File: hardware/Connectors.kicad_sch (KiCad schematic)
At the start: 9 parts, among them J1 Harw_Conn_1x2, J10 USB_B_Mini, J14 Conn_01x05, J16 Harw_Conn_2x13, J2 Harw_Conn_1x2, J3 Harw_Conn_1x2, J8 Harw_Conn_1x4

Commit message: finished board design
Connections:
- net AMS_FAULT_COCKPIT: now also J16.10; no longer J16.22
- net AMS_SAFETY_1: now also J16.9; no longer J16.24
- net AMS_SAFETY_2: now also J16.22; no longer J16.9
- net CAN_H: now also J16.24; no longer J16.10
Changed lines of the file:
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@@
     (stroke (width 0) (type default) (color 0 0 0 0))
   )
-  (wire (pts (xy 84.455 121.92) (xy 81.915 121.92))
+  (wire (pts (xy 66.675 116.84) (xy 69.215 116.84))
     (stroke (width 0) (type default) (color 0 0 0 0))
   )
@@
     (stroke (width 0) (type default) (color 0 0 0 0))
   )
+  (wire (pts (xy 84.455 121.92) (xy 81.915 121.92))
+    (stroke (width 0) (type default) (color 0 0 0 0))
+  )
+  (wire (pts (xy 240.665 63.5) (xy 240.665 64.77))
+    (stroke (width 0) (type default) (color 0 0 0 0))
+  )
+  (wire (pts (xy 250.825 46.99) (xy 250.825 43.18))
+    (stroke (width 0) (type default) (color 0 0 0 0))
+  )
+  (wire (pts (xy 180.975 137.16) (xy 178.435 137.16))
+    (stroke (width 0) (type default) (color 0 0 0 0))
+  )
+  (wire (pts (xy 250.19 111.76) (xy 250.19 113.03))
+    (stroke (width 0) (type default) (color 0 0 0 0))
+  )
+  (wire (pts (xy 179.705 134.62) (xy 179.705 132.08))
+    (stroke (width 0) (type default) (color 0 0 0 0))
+  )
+  (wire (pts (xy 240.665 63.5) (xy 241.935 63.5))
+    (stroke (width 0) (type default) (color 0 0 0 0))
+  )
+  (wire (pts (xy 66.675 104.14) (xy 69.215 104.14))
+    (stroke (width 0) (type default) (color 0 0 0 0))
+  )
+  (wire (pts (xy 69.215 121.92) (xy 66.675 121.92))
+    (stroke (width 0) (type default) (color 0 0 0 0))
+  )
+  (wire (pts (xy 172.72 81.915) (xy 175.26 81.915))
+    (stroke (width 0) (type default) (color 0 0 0 0))
+  )
+  (wire (pts (xy 188.595 47.625) (xy 186.055 47.625))
+    (stroke (width 0) (type default) (color 0 0 0 0))
+  )
+  (wire (pts (xy 249.555 46.99) (xy 250.825 46.99))
+    (stroke (width 0) (type default) (color 0 0 0 0))
+  )
+  (wire (pts (xy 248.92 106.045) (xy 251.46 106.045))
+    (stroke (width 0) (type default) (color 0 0 0 0))
+  )
+  (wire (pts (xy 184.785 48.895) (xy 186.055 48.895))
+    (stroke (width 0) (type default) (color 0 0 0 0))
+  )
   (wire (pts (xy 66.675 119.38) (xy 69.215 119.38))
-    (stroke (width 0) (type default) (color 0 0 0 0))
-  )
-  (wire (pts (xy 240.665 63.5) (xy 240.665 64.77))
-    (stroke (width 0) (type default) (color 0 0 0 0))
-  )
-  (wire (pts (xy 250.825 46.99) (xy 250.825 43.18))
-    (stroke (width 0) (type default) (color 0 0 0 0))
-  )
-  (wire (pts (xy 180.975 137.16) (xy 178.435 137.16))
-    (stroke (width 0) (type default) (color 0 0 0 0))
-  )
-  (wire (pts (xy 250.19 111.76) (xy 250.19 113.03))
-    (stroke (width 0) (type default) (color 0 0 0 0))
-  )
-  (wire (pts (xy 179.705 134.62) (xy 179.705 132.08))
-    (stroke (width 0) (type default) (color 0 0 0 0))
-  )
-  (wire (pts (xy 240.665 63.5) (xy 241.935 63.5))
-    (stroke (width 0) (type default) (color 0 0 0 0))
-  )
-  (wire (pts (xy 66.675 104.14) (xy 69.215 104.14))
-    (stroke (width 0) (type default) (color 0 0 0 0))
-  )
-  (wire (pts (xy 69.215 121.92) (xy 66.675 121.92))
-    (stroke (width 0) (type default) (color 0 0 0 0))
-  )
-  (wire (pts (xy 172.72 81.915) (xy 175.26 81.915))
-    (stroke (width 0) (type default) (color 0 0 0 0))
-  )
-  (wire (pts (xy 188.595 47.625) (xy 186.055 47.625))
-    (stroke (width 0) (type default) (color 0 0 0 0))
-  )
-  (wire (pts (xy 249.555 46.99) (xy 250.825 46.99))
-    (stroke (width 0) (type default) (color 0 0 0 0))
-  )
-  (wire (pts (xy 248.92 106.045) (xy 251.46 106.045))
-    (stroke (width 0) (type default) (color 0 0 0 0))
-  )
-  (wire (pts (xy 184.785 48.895) (xy 186.055 48.895))
-    (stroke (width 0) (type default) (color 0 0 0 0))
-  )
-  (wire (pts (xy 84.455 116.84) (xy 81.915 116.84))
     (stroke (width 0) (type default) (color 0 0 0 0))
   )
@@
     (stroke (width 0) (type default) (color 0 0 0 0))
   )
-  (wire (pts (xy 69.215 116.84) (xy 66.675 116.84))
+  (wire (pts (xy 81.915 116.84) (xy 84.455 116.84))
     (stroke (width 0) (type default) (color 0 0 0 0))
   )
@@
     )
   )
-  (global_label "CAN_H" (shape input) (at 66.675 119.38 180) (fields_autoplaced)
-    (effects (font (size 1.27 1.27)) (justify right))
-    (property "Intersheet References" "${INTERSHEET_REFS}" (id 0) (at 58.3637 119.4594 0)
-      (effects (font (size 1.27 1.27)) (justify right) hide)
+  (global_label "CAN_H" (shape input) (at 84.455 121.92 0) (fields_autoplaced)
+    (effects (font (size 1.27 1.27)) (justify left))
+    (property "Intersheet References" "${INTERSHEET_REFS}" (id 0) (at 92.7663 121.8406 0)
+      (effects (font (size 1.27 1.27)) (justify left) hide)
     )
   )
@@
     )
   )
-  (global_label "AMS_FAULT_COCKPIT" (shape input) (at 84.455 116.84 0) (fields_autoplaced)
-    (effects (font (size 1.27 1.27)) (justify left))
-    (property "Intersheet References" "${INTERSHEET_REFS}" (id 0) (at 105.9502 116.7606 0)
-      (effects (font (size 1.27 1.27)) (justify left) hide)
+  (global_label "AMS_FAULT_COCKPIT" (shape input) (at 66.675 119.38 180) (fields_autoplaced)
+    (effects (font (size 1.27 1.27)) (justify right))
+    (property "Intersheet References" "${INTERSHEET_REFS}" (id 0) (at 45.1798 119.4594 0)
+      (effects (font (size 1.27 1.27)) (justify right) hide)
     )
   )
@@
     )
   )
-  (global_label "AMS_SAFETY_2" (shape input) (at 66.675 116.84 180) (fields_autoplaced)
+  (global_label "AMS_SAFETY_2" (shape input) (at 84.455 116.84 0) (fields_autoplaced)
+    (effects (font (size 1.27 1.27)) (justify left))
+    (property "Intersheet References" "${INTERSHEET_REFS}" (id 0) (at 100.2654 116.7606 0)
+      (effects (font (size 1.27 1.27)) (justify left) hide)
+    )
+  )
+  (global_label "SWDIO" (shape input) (at 178.435 142.24 180) (fields_autoplaced)
+    (effects (font (size 1.27 1.27)) (justify right))
+    (property "Intersheet References" "${INTERSHEET_REFS}" (id 0) (at 170.2446 142.1606 0)
+      (effects (font (size 1.27 1.27)) (justify right) hide)
+    )
+  )
+  (global_label "AIR_M" (shape input) (at 66.675 111.76 180) (fields_autoplaced)
+    (effects (font (size 1.27 1.27)) (justify right))
+    (property "Intersheet References" "${INTERSHEET_REFS}" (id 0) (at 58.9684 111.8394 0)
+      (effects (font (size 1.27 1.27)) (justify right) hide)
+    )
+  )
+  (global_label "AMS_SAFETY_1" (shape input) (at 66.675 116.84 180) (fields_autoplaced)
     (effects (font (size 1.27 1.27)) (justify right))
     (property "Intersheet References" "${INTERSHEET_REFS}" (id 0) (at 50.8646 116.9194 0)
@@
     )
   )
-  (global_label "SWDIO" (shape input) (at 178.435 142.24 180) (fields_autoplaced)
-    (effects (font (size 1.27 1.27)) (justify right))
-    (property "Intersheet References" "${INTERSHEET_REFS}" (id 0) (at 170.2446 142.1606 0)
-      (effects (font (size 1.27 1.27)) (justify right) hide)
-    )
-  )
-  (global_label "AIR_M" (shape input) (at 66.675 111.76 180) (fields_autoplaced)
-    (effects (font (size 1.27 1.27)) (justify right))
-    (property "Intersheet References" "${INTERSHEET_REFS}" (id 0) (at 58.9684 111.8394 0)
-      (effects (font (size 1.27 1.27)) (justify right) hide)
-    )
-  )
-  (global_label "AMS_SAFETY_1" (shape input) (at 84.455 121.92 0) (fields_autoplaced)
-    (effects (font (size 1.27 1.27)) (justify left))
-    (property "Intersheet References" "${INTERSHEET_REFS}" (id 0) (at 100.2654 121.8406 0)
-      (effects (font (size 1.27 1.27)) (justify left) hide)
-    )
-  )

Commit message: schematic override, just cuz
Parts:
- removed J1: Harw_Conn_1x2, M808420245, symbol Harwin 2 pin 90 deg:Harw_Conn_1x2
- removed J10: USB_B_Mini, Connector_USB:USB_Mini-B_Lumberg_2486_01_Horizontal, symbol Connector:USB_B_Mini
- removed R46: 100k, Resistor_SMD:R_0603_1608Metric, symbol Device:R_Small
- added P3: USB_C_Plug_USB2.0, Connector_USB:USB_C_Receptacle_HRO_TYPE-C-31-M-12, symbol Connector:USB_C_Plug_USB2.0
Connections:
- net D+: now also J8.3, P3.A6 (D+); no longer J8.2
- net D-: now also J8.2, P3.A7 (D-); no longer J8.3
- net GND: now also J16.14, J16.15; no longer J16.17, J16.19, J16.8
- net LTC_1_CHASSIS: no longer J16.16
- net LTC_1_OUT_I+: no longer J16.14
- net LTC_1_OUT_I-: no longer J16.1
- net LTC_2_CHASSIS: no longer J16.3
- net LTC_2_OUT_I+: no longer J16.15
- net LTC_2_OUT_I-: no longer J16.2
- net SENSOR_SIGNAL: no longer J16.4
- net USB_GND: now also P3.A1 (GND), P3.A12 (GND), P3.B1 (GND), P3.B12 (GND)
- net VBUS: now also P3.A4 (VBUS), P3.A9 (VBUS), P3.B4 (VBUS), P3.B9 (VBUS)
- net VDD: now also J16.1; no longer J16.21
- net at F1.2: now also J16.2; no longer J16.5
- net HV_ACU_VOLTAGE renamed HV_ACU+
- net HV_ACU+: no longer J3.2
- net HV_CAR_VOLTAGE renamed HV_CAR+
- net HV_CAR+: no longer J2.2
- new net HV_ACU-: J3.2
- new net HV_CAR-: J2.2
- no-connect marks 0 -> 3
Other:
- moved on the sheet: F1

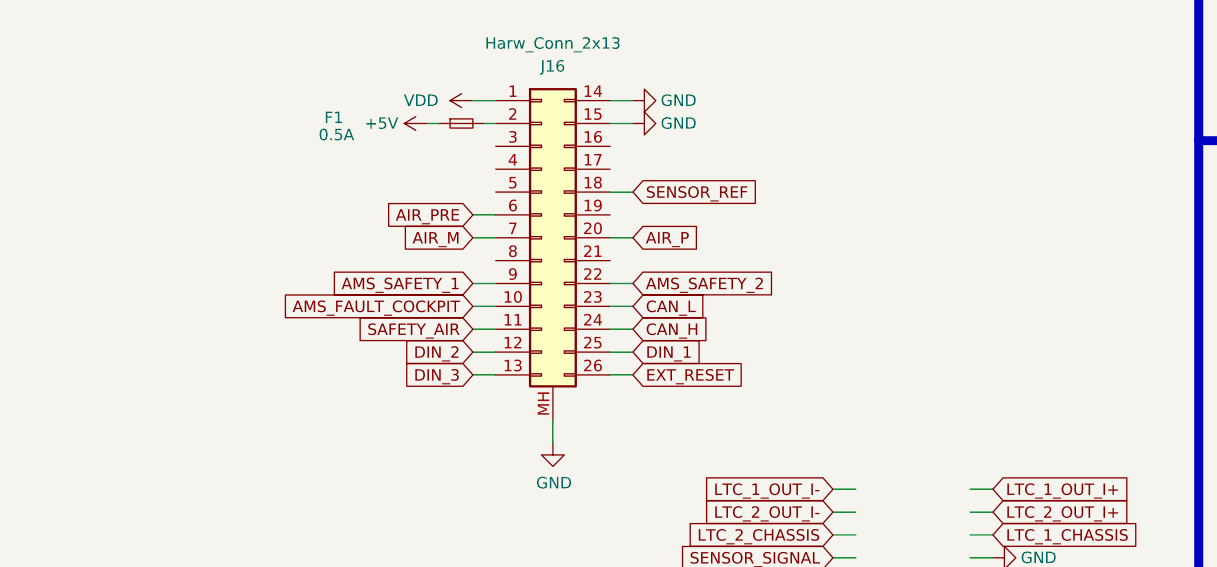
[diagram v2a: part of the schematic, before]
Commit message: changed HV measurements from isolated opamp to isolated ADC with isolated spi communication, changed safety laatching from mosfet back to relay
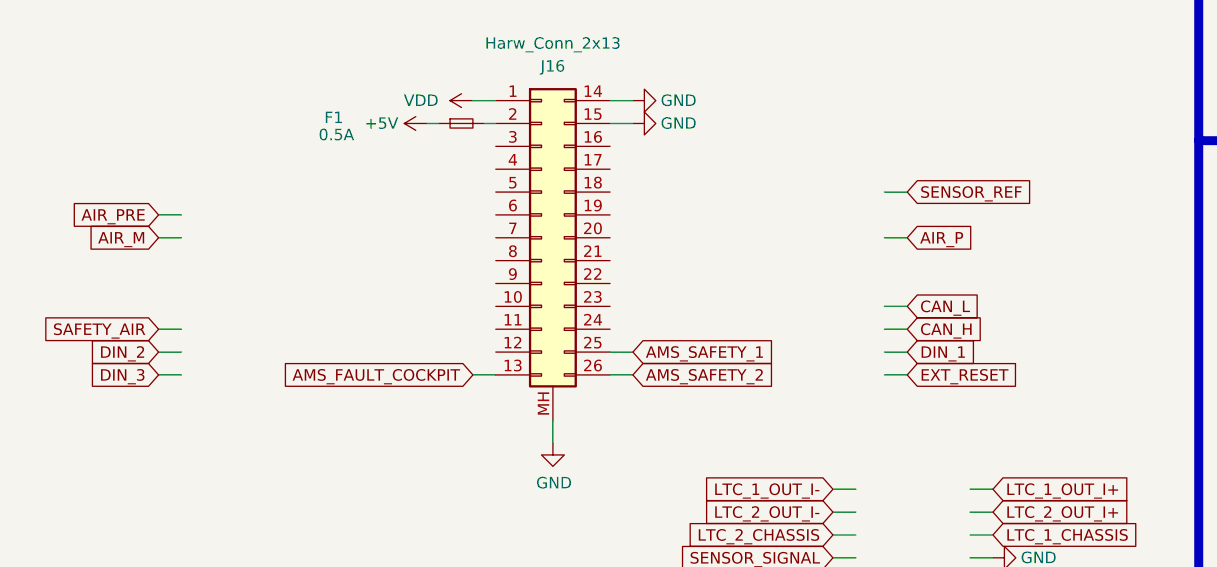
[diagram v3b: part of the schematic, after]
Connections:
- net AIR_M: no longer J16.7
- net AIR_P: no longer J16.20
- net AIR_PRE: no longer J16.6
- net AMS_FAULT_COCKPIT: now also J16.13; no longer J16.10
- net AMS_SAFETY_1: now also J16.25; no longer J16.9
- net AMS_SAFETY_2: now also J16.26; no longer J16.22
- net CAN_H: no longer J16.24
- net CAN_L: no longer J16.23
- net DIN_1: no longer J16.25
- net DIN_2: no longer J16.12
- net DIN_3: no longer J16.13
- net EXT_RESET: no longer J16.26
- net SAFETY_AIR: no longer J16.11
- net SENSOR_REF: no longer J16.18

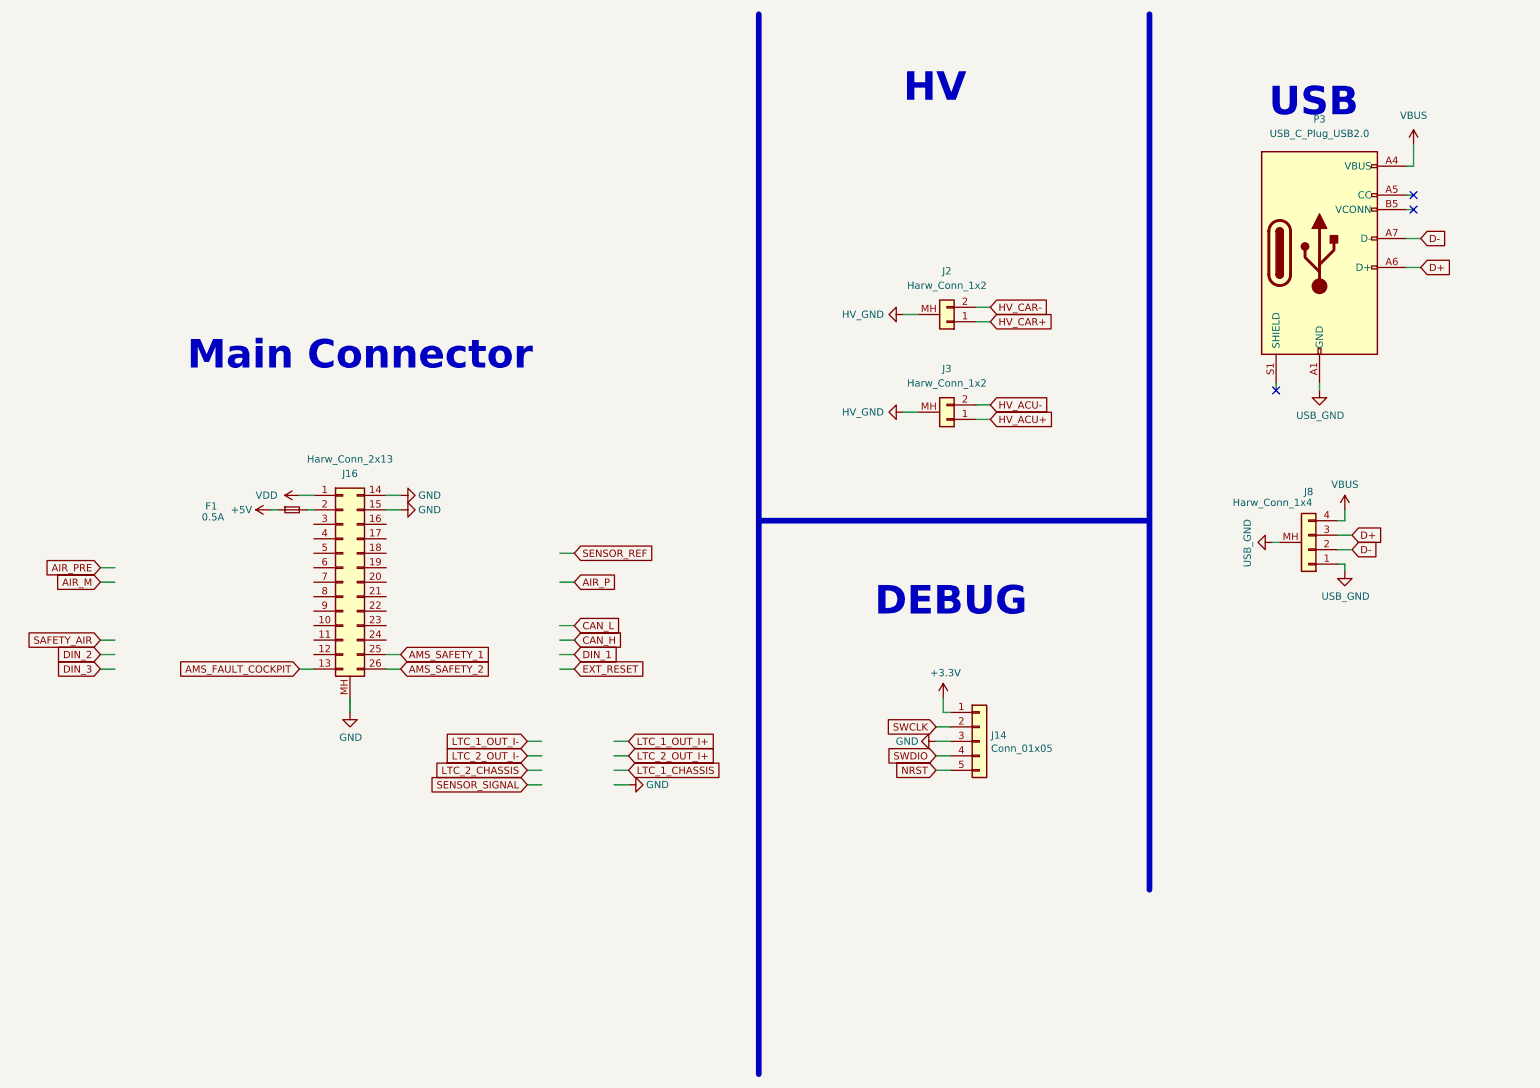
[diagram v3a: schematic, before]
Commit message: changed the 1V voltage ref made from RL circuit to low noise, 0.1% error 1.024 V ref gen, and changed the opamp used for current sensor feedback filtration to a high precision low drift opamp
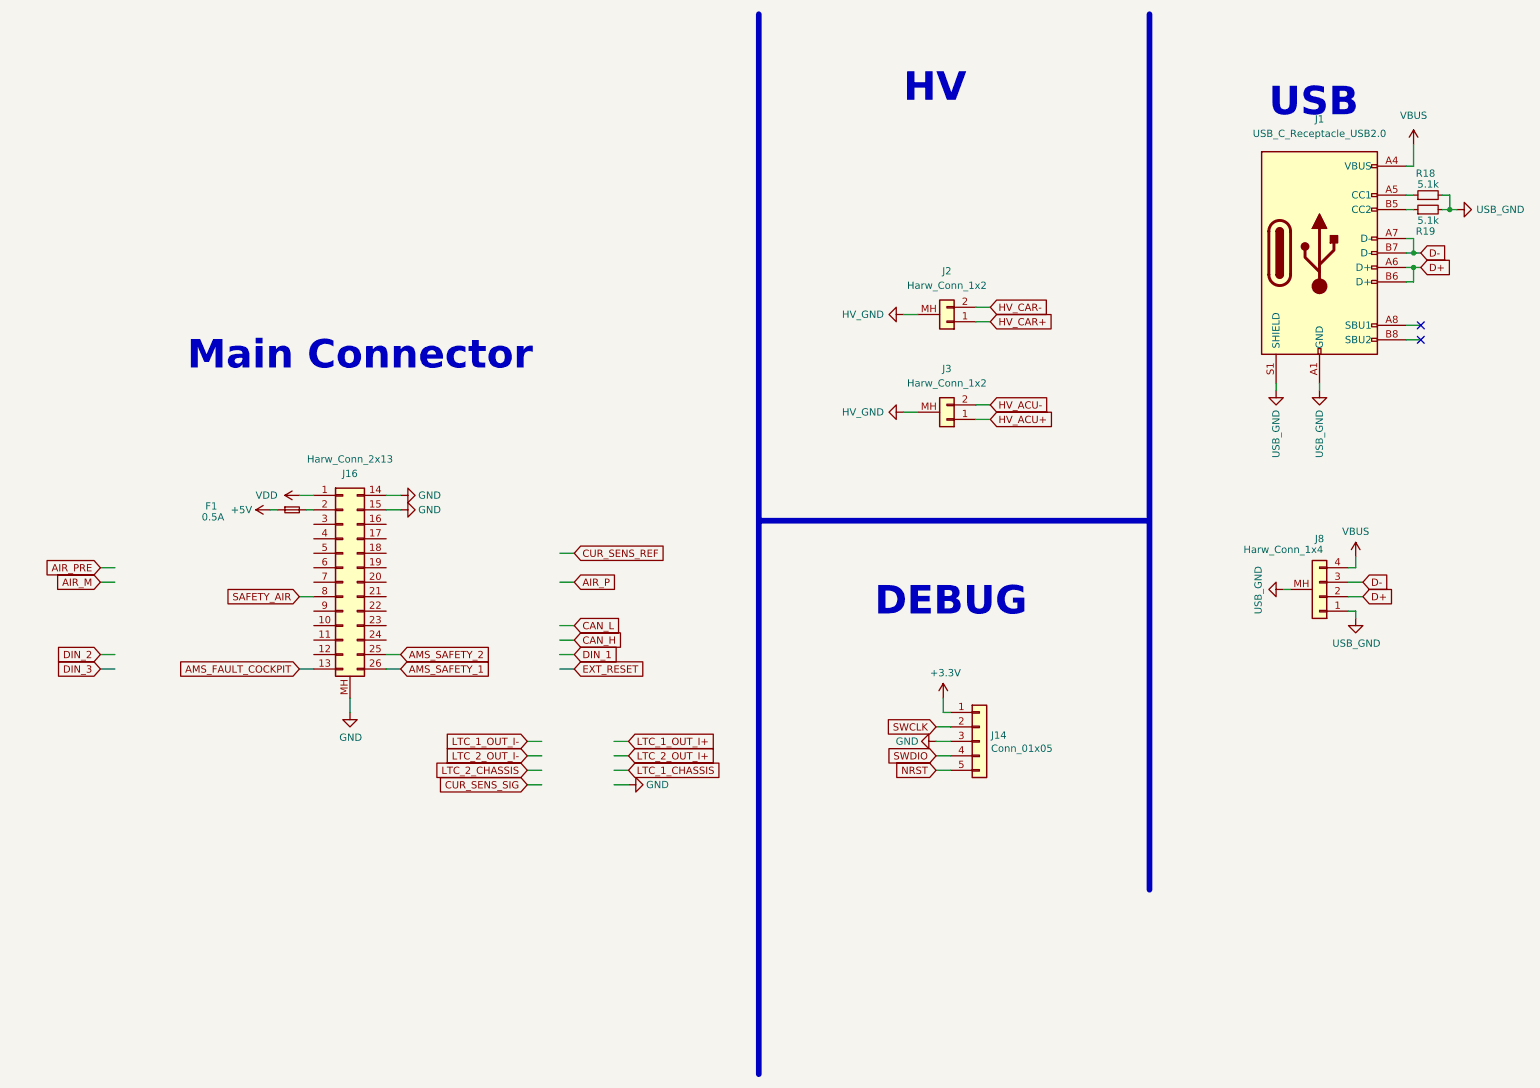
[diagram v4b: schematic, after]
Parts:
- removed P3: USB_C_Plug_USB2.0, Connector_USB:USB_C_Receptacle_HRO_TYPE-C-31-M-12, symbol Connector:USB_C_Plug_USB2.0
- added J1: USB_C_Receptacle_USB2.0, Connector_USB:USB_C_Receptacle_HRO_TYPE-C-31-M-12, symbol Connector:USB_C_Receptacle_USB2.0
- added R18, R19: 5.1k, Resistor_SMD:R_0603_1608Metric, symbol Device:R_Small
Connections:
- net AMS_SAFETY_1: now also J16.26; no longer J16.25
- net AMS_SAFETY_2: now also J16.25; no longer J16.26
- net D+: now also J8.2, J1.A6 (D+), J1.B6 (D+); no longer J8.3
- net D-: now also J8.3, J1.A7 (D-), J1.B7 (D-); no longer J8.2
- net SAFETY_AIR: now also J16.8
- net USB_GND: now also J1.A1 (GND), J1.A12 (GND), J1.B1 (GND), J1.B12 (GND), J1.S1 (SHIELD), R18.2, R19.2
- net VBUS: now also J1.A4 (VBUS), J1.A9 (VBUS), J1.B4 (VBUS), J1.B9 (VBUS)
- new net: J1.A5 (CC1), R18.1
- new net: J1.B5 (CC2), R19.1
- no-connect marks 3 -> 2
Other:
- moved on the sheet: J8
